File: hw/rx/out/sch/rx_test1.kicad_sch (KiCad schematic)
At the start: 13 parts

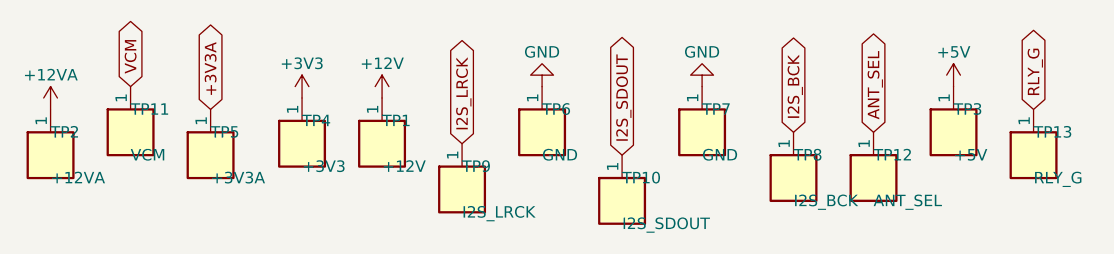
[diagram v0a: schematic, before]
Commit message: hw/rx + hw/pack: #116 review fixes: netclass pour clearances (no 0.09 mm override), keyed J1 with no hole at 14, solid RF grounds, K1 pin-1/CPL rotation, raw RF numbers (#34)
- M1: JLC copper-clearance rule removed from rx and pack .kicad_dru; boards refilled/regenerated; probe-rule tests
  assert >= 0.125 mm everywhere and >= 0.15 mm to Audio_I on the committed fill; outer-copper rule width-independent
- S1: openpack:PinHeader_2x13_P2.54mm_Key14 (pad 14 deleted, KEY silk), header XFCN PZ254V-12-26P (LCSC C22465887,
  pin 14 cut), main-board socket Samtec SSW-113-01-G-D-14 recorded in ADR-0014; test
- S2: zone_connect solid on J3-J5, U2, U1 GND pads; test
- S3: TQ2SA pin-1 dot + '+', CPL +270 for the relay (K1 at 180); pin-1 marker + CPL test for all polarized parts
- N1 raw RF Z0 (51.5 bare / ~49.3 masked), N3 C44 at U6, REVIEW follow-ups

Co-Authored-By: Claude Opus 5.5 <noreply@anthropic.com>
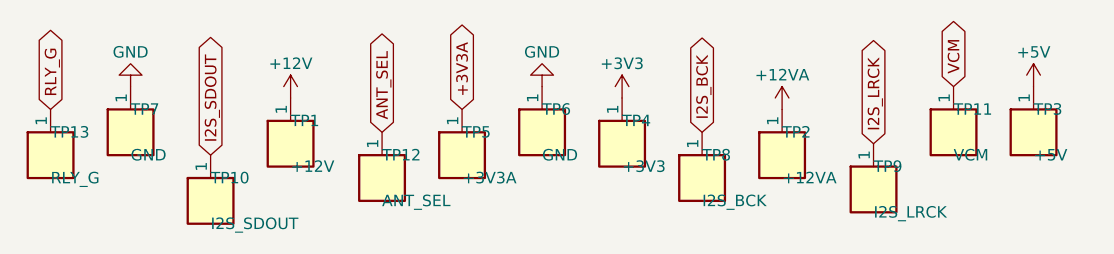
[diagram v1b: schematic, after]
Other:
- moved on the sheet: TP1, TP10, TP11, TP12, TP13, TP2, TP3, TP4, TP5, TP7, TP8, TP9
